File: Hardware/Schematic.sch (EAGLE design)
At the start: 103 parts, among them IC1 XC6220A331MR-G, IC2 BD5229G-TR, J1 SAMACSYS_PARTS_USB4110-GF-A, J2 FH34SRJ-24S-0.5SH_99_, J3 QWIIC_RIGHT_ANGLE, J4 112A-TAAR-R03_ATTEND, Q1 20V/4.2A/52mΩ/1.4W, Q2 SI1308EDL-T1-GE3, Q3 20V/4.2A/52mΩ/1.4W, U1 ESP32_WROVER_SPARKFUN-IC-POWE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, U2 ESP32-C6-WROOM-1-N8, U3 ESP32_WROVER_BME680_BME680, U4 MAX17048G+T10, U5 DS3231SN#, U6 W25Q512JVEIQ

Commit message: solved all issues raised
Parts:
- removed U5: DS3231SN#, DeskAssistant v19 v1.flbr:DS3231SN#
- removed U6: W25Q512JVEIQ, DeskAssistant v19 v1.flbr:W25Q512JVEIQ
- added U10: ESP32_WROVER_BME680_BME680, DeskAssistant v19 v1.flbr:ESP32_WROVER_BME680_BME680
- added U9: ESP32_WROVER_SPARKFUN-IC-POWER_MCP73831, DeskAssistant v19 v1.flbr:ESP32_WROVER_SPARKFUN-IC-POWER_MCP73831
- D6: value ESP32_WROVER_AVX---SD0805S020S1R0_AVX_SD0805S020S1R0_0_0AVX_SD0805S020S1R0_0_0 -> PGB1010603MR; device DeskAssistant v19 v1.flbr:ESP32_WROVER_AVX---SD0805S020S1R0_AVX_SD0805S020S1R0_0_0AVX_SD0805S020S1R0_0_0 -> DeskAssistant v19 v1.flbr:PGB1010603MR
- D7: value PGB1010603MR -> ESP32_WROVER_AVX---SD0805S020S1R0_AVX_SD0805S020S1R0_0_0AVX_SD0805S020S1R0_0_0; device DeskAssistant v19 v1.flbr:PGB1010603MR -> DeskAssistant v19 v1.flbr:ESP32_WROVER_AVX---SD0805S020S1R0_AVX_SD0805S020S1R0_0_0AVX_SD0805S020S1R0_0_0
- Q2: value SI1308EDL-T1-GE3 -> 20V/4.2A/52mΩ/1.4W; device DeskAssistant v19 v1.flbr:SI1308EDL-T1-GE3 -> DeskAssistant v19 v1.flbr:ESP32_WROVER_SPARKFUN-DISCRETESEMI_MOSFET_PCH-DMG2305UX-7
- Q3: value 20V/4.2A/52mΩ/1.4W -> SI1308EDL-T1-GE3; device DeskAssistant v19 v1.flbr:ESP32_WROVER_SPARKFUN-DISCRETESEMI_MOSFET_PCH-DMG2305UX-7 -> DeskAssistant v19 v1.flbr:SI1308EDL-T1-GE3
- U1: value ESP32_WROVER_SPARKFUN-IC-POWER_MCP73831 -> W25Q512JVEIQ; device DeskAssistant v19 v1.flbr:ESP32_WROVER_SPARKFUN-IC-POWER_MCP73831 -> DeskAssistant v19 v1.flbr:W25Q512JVEIQ
- U3: value ESP32_WROVER_BME680_BME680 -> DS3231SN#; device DeskAssistant v19 v1.flbr:ESP32_WROVER_BME680_BME680 -> DeskAssistant v19 v1.flbr:DS3231SN#
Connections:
- net 32KHZ: now also U3.32KHZ; no longer U5.32KHZ
- net 3V3: now also D7.ANODE, Q2.D, U1.!HOLD!/!RESET!(IO3), U1.!WP!(IO2), U1.VCC, U3.VCC; no longer D6.ANODE, Q3.D, U5.VCC, U6.!HOLD!/!RESET!(IO3), U6.!WP!(IO2), U6.VCC
- net EPD_3V3: now also Q2.S; no longer Q3.S
- net EPD_3V3_C: now also Q2.G; no longer Q3.G
- net EPD_CS: now also D6.2; no longer D11.2
- net FLASH_CS: now also D9.2, U1.!CS; no longer D10.2, U6.!CS
- net GDR: now also Q3.G; no longer Q2.G
- net GND: now also D3.K, D6.1, EPD_C2.1, U1.EXP, U1.GND, U10.GND, U10.SDO, U9.VSS; no longer D4.K, D7.1, U1.VSS, U3.SDO, U5.GND, U6.EXP, U6.GND
- net I2C_PW: now also U10.CSB, U10.VDD, U10.VDDIO; no longer U3.CSB, U3.VDD, U3.VDDIO
- net INT_RTC: now also U3.SQW/!INT; no longer U5.SQW/!INT
- net MISO: now also D12.2, U1.DO(IO1); no longer D7.2, U6.DO(IO1)
- net MOSI: now also D11.2, U1.DI(IO0); no longer D8.2, U6.DI(IO0)
- net N$21: now also D7.CATHODE; no longer D6.CATHODE
- net N$4: now also D3.A, D4.K; no longer D3.K, D4.A
- net N$5: now also U9.PROG; no longer U1.PROG
- net N$7: now also U9.STAT; no longer U1.STAT
- net PREVGL: now also D4.A; no longer D3.A
- net RESE: now also Q3.S; no longer Q2.S
- net RTC_RST: now also U3.!RST; no longer U5.!RST
- net SCK: now also D10.2, U1.CLK; no longer D9.2, U6.CLK
- net SCL: now also U10.SCK, U3.SCL; no longer U3.SCK, U5.SCL
- net SDA: now also U10.SDI, U3.SDA; no longer U3.SDI, U5.SDA
- net SRC: now also Q3.D; no longer Q2.D
- net SS_SD: now also D8.2; no longer D12.2
- net VBAT: now also U9.VBAT; no longer U1.VBAT
- net VBUS: now also U9.VIN; no longer U1.VIN
- net VRTC: now also U3.VBAT; no longer U5.VBAT
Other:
- note added: "8:31 AM 11/04/2025"
- note removed: "9:41 AM 24/03/2024"
- moved on the sheet: D10, D11, D12, D3, D4, D8, D9

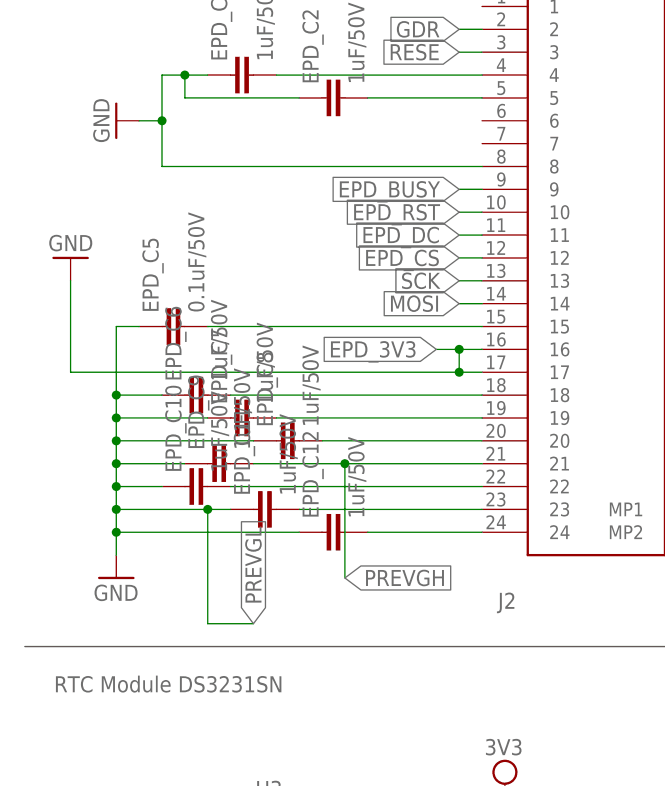
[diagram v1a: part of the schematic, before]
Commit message: fix erc issues
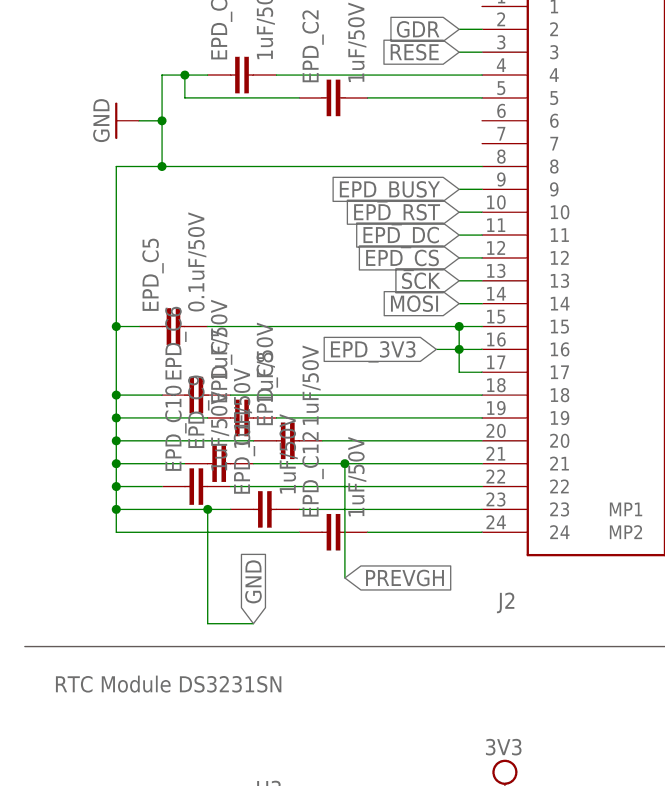
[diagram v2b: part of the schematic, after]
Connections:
- removed net N$11: EPD_C5.2, J2.15
- net EPD_3V3: now also EPD_C5.2, J2.15
- net GND: now also EPD_C10.1, EPD_C11.1, EPD_C12.1, EPD_C5.1, EPD_C6.1, EPD_C7.1, EPD_C8.1, EPD_C9.1
- net PREVGL: no longer EPD_C10.1, EPD_C11.1, EPD_C12.1, EPD_C5.1, EPD_C6.1, EPD_C7.1, EPD_C8.1, EPD_C9.1
